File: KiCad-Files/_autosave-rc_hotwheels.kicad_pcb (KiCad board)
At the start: 2 copper layers, 29.5 x 21.6 mm, 16 parts, among them IC1 BD6211F-E2, IC2 MIC5504-3.3YM5-TR, M1 Motor_Connection, U1 STM32F070F6P6, U3 NRF24L01_Breakout

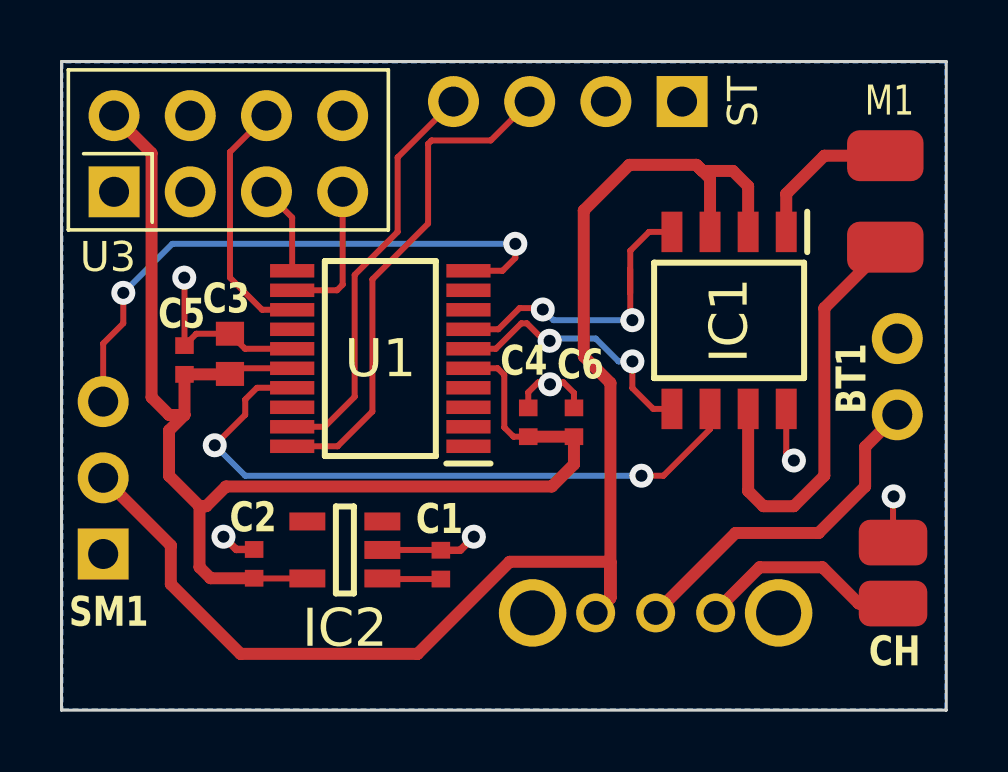
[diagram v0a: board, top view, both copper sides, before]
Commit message: Updated all power traces
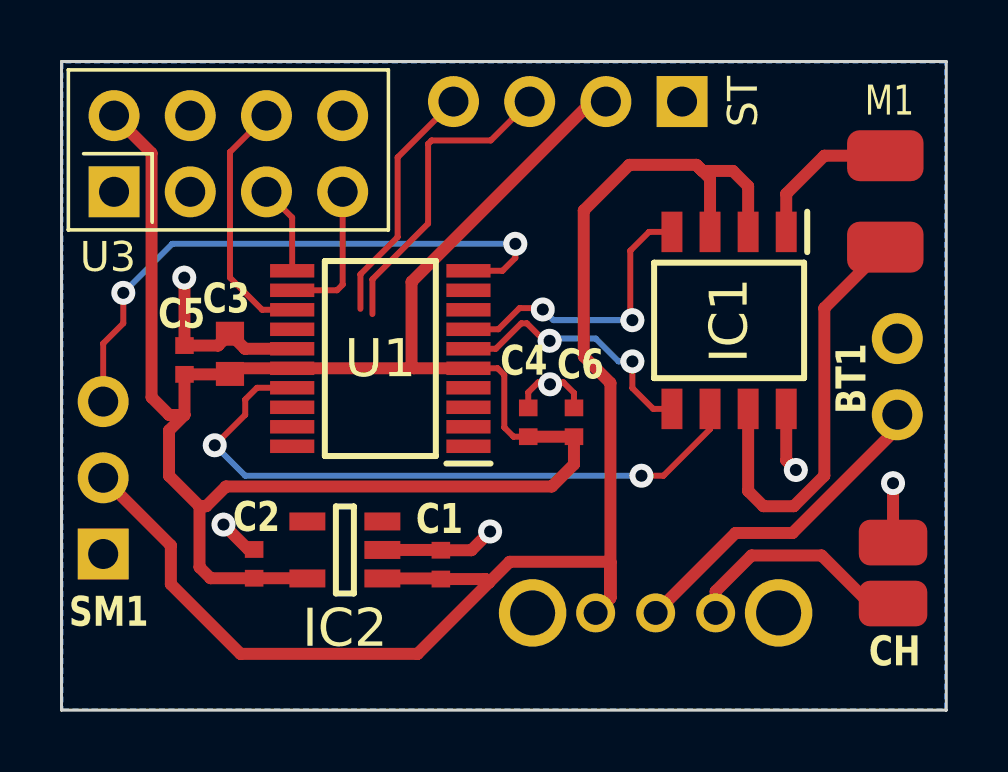
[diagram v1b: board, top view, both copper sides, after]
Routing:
- net VR_OUT: track 45.2 -> 62.9 mm
- net SYS_SWCLK: track 16.8 -> 10.4 mm
- net SYS_SWDIO: track 13.7 -> 8.20 mm
- net VCC: track 48.9 -> 50.6 mm
- net GND: track 16.9 -> 18.4 mm
- net Motor Forward: track 10.7 -> 9.92 mm
- net Net-(S3-BATT+): track 7.08 -> 7.79 mm
- net Net-(BT1-+): track 11.6 -> 11.1 mm
